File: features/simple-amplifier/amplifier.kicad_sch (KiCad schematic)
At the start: 7 parts, among them Q1 BC846

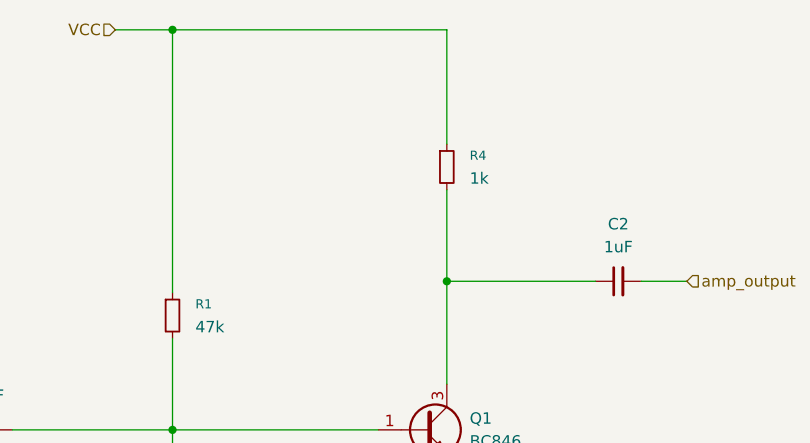
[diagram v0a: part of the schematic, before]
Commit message: feat(simple-amplifier): add collector resistor
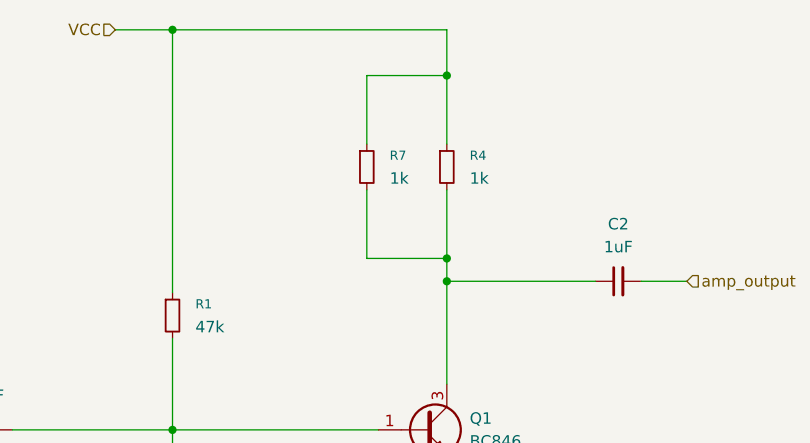
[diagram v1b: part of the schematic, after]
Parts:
- added R7: 1k, Resistor_SMD:R_0603_1608Metric, symbol Device:R_Small
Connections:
- net VCC: now also R7.1
- net at C2.1, Q1.3 (C), R4.2: now also R7.2
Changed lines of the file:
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@@
+	)
+	(junction
+		(at 163.83 81.28)
+		(diameter 0)
+		(color 0 0 0 0)
 	)
 	(junction
@@
 		(color 0 0 0 0)
 	)
+	(junction
+		(at 163.83 60.96)
+		(diameter 0)
+		(color 0 0 0 0)
+	)
 	(wire
 		(pts
@@
 	(wire
 		(pts
-			(xy 163.83 73.66) (xy 163.83 83.82)
+			(xy 163.83 73.66) (xy 163.83 81.28)
 		)
 		(stroke
@@
 	(wire
 		(pts
+			(xy 154.94 60.96) (xy 163.83 60.96)
+		)
+		(stroke
+			(width 0)
+			(type default)
+		)
+	)
+	(wire
+		(pts
+			(xy 163.83 81.28) (xy 163.83 83.82)
+		)
+		(stroke
+			(width 0)
+			(type default)
+		)
+	)
+	(wire
+		(pts
 			(xy 133.35 100.33) (xy 156.21 100.33)
 		)
@@
 	(wire
 		(pts
+			(xy 154.94 73.66) (xy 154.94 81.28)
+		)
+		(stroke
+			(width 0)
+			(type default)
+		)
+	)
+	(wire
+		(pts
 			(xy 185.42 83.82) (xy 190.5 83.82)
 		)
@@
 	(wire
 		(pts
-			(xy 163.83 55.88) (xy 163.83 68.58)
+			(xy 163.83 55.88) (xy 163.83 60.96)
+		)
+		(stroke
+			(width 0)
+			(type default)
+		)
+	)
+	(wire
+		(pts
+			(xy 163.83 60.96) (xy 163.83 68.58)
+		)
+		(stroke
+			(width 0)
+			(type default)
+		)
+	)
+	(wire
+		(pts
+			(xy 154.94 68.58) (xy 154.94 60.96)
 		)
 		(stroke
@@
 		(pts
 			(xy 163.83 83.82) (xy 180.34 83.82)
+		)
+		(stroke
+			(width 0)
+			(type default)
+		)
+	)
+	(wire
+		(pts
+			(xy 154.94 81.28) (xy 163.83 81.28)
 		)
 		(stroke
@@
 					(unit 1)
 				)
+			)
+		)
+	)
+	(symbol
+		(lib_id "Device:R_Small")
+		(at 154.94 71.12 0)
+		(unit 1)
+		(body_style 1)
+		(exclude_from_sim no)
+		(in_bom yes)
+		(on_board yes)
+		(in_pos_files yes)
+		(dnp no)
+		(fields_autoplaced yes)
+		(property "Reference" "R7"
+			(at 157.48 69.8499 0)
+			(show_name no)
+			(do_not_autoplace no)
+			(effects
+				(font
+					(size 1.016 1.016)
+				)
+				(justify left)
+			)
+		)
+		(property "Value" "1k"
+			(at 157.48 72.3899 0)
+			(show_name no)
+			(do_not_autoplace no)
+			(effects
+				(font
+					(size 1.27 1.27)
+				)
+				(justify left)
+			)
+		)
+		(property "Footprint" "Resistor_SMD:R_0603_1608Metric"
+			(at 154.94 71.12 0)
+			(hide yes)
+			(show_name no)
+			(do_not_autoplace no)
+			(effects
+				(font
+					(size 1.27 1.27)
+				)
+			)
+		)
+		(property "Datasheet" ""
+			(at 154.94 71.12 0)
+			(hide yes)
+			(show_name no)
+			(do_not_autoplace no)
+			(effects
+				(font
+					(size 1.27 1.27)
+				)
+			)
+		)
+		(property "Description" "Resistor, small symbol"
+			(at 154.94 71.12 0)
+			(hide yes)
+			(show_name no)
+			(do_not_autoplace no)
+			(effects
+				(font
+					(size 1.27 1.27)
+				)
+			)
+		)
+		(pin "2"
+		)
+		(pin "1"
+		)
+		(instances
+			(project "simple-amplifier"
+				(path "/b5096a5b-7eb5-4b6d-ab4d-f26b7572c575/7cab90dc-3b93-4f7f-826b-dd55670e1a17"
+					(reference "R7")
+					(unit 1)
+				)
